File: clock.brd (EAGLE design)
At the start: 100 x 80 mm, 46 parts, among them J3 POWER_JACKSLT, U2 LM75A_SO8, U3 ESP8266_13

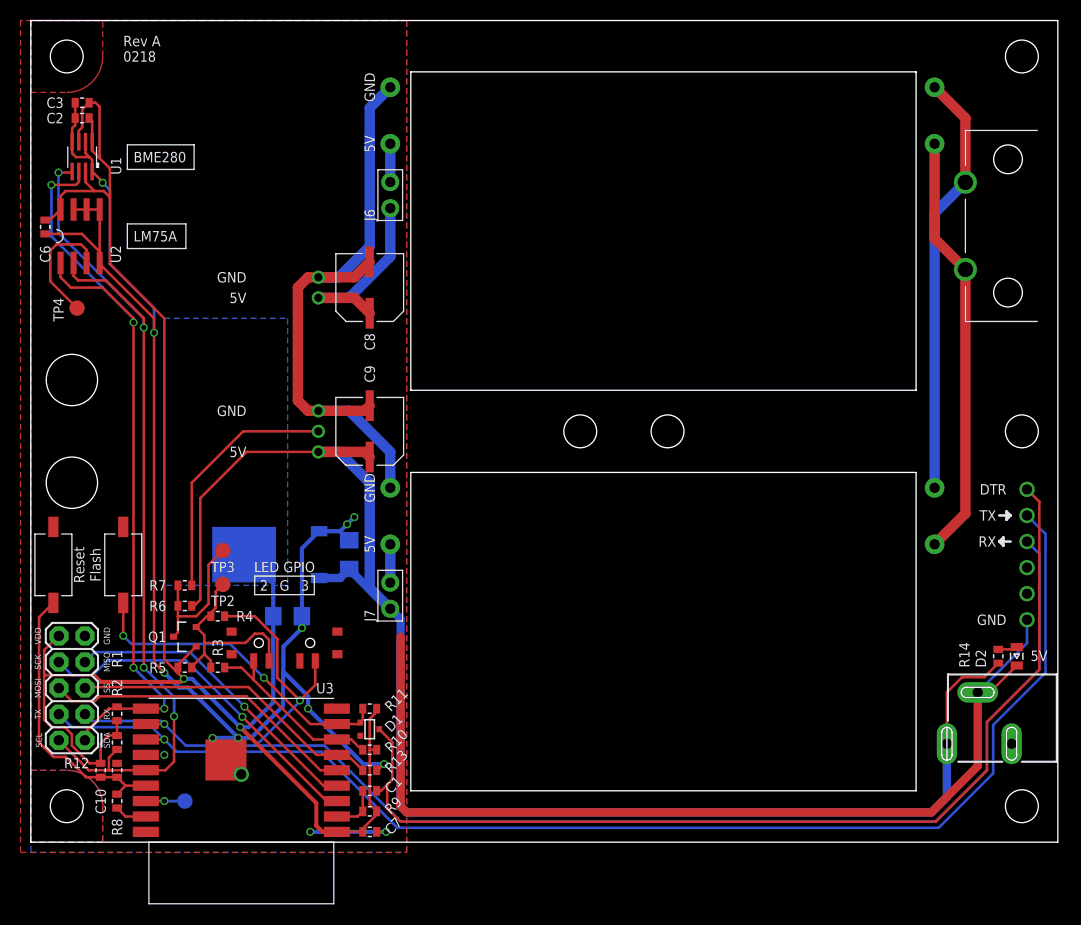
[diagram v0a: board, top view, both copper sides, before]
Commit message: Added a status LED to IO0
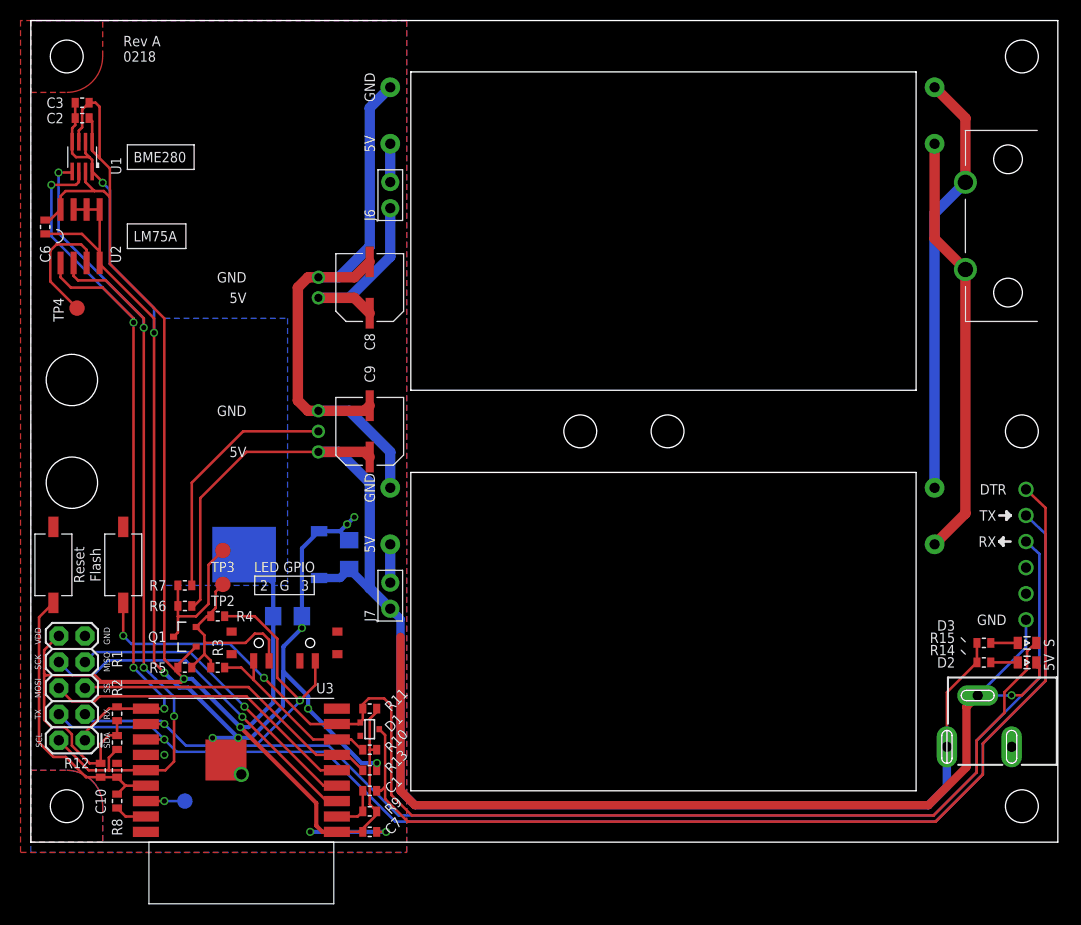
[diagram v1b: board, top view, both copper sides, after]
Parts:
- added D3: (no value), Sebastian:0805_LED
- added R15: 1k, Sebastian:0603
- moved R14 1.52 mm to (92.8, 17.5), turned to 180 degrees
- moved D2 1.17 mm to (97.0, 17.5), turned to 0 degrees
- moved J3 0.30 mm to (103.0, 6.70)
- moved J1 0.10 mm to (96.9, 28.0)
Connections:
- new net N$5: D3.A, R15.1
- net IO0: now also D3.C
- net PVDD: now also R15.2
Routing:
- net IO0: track 31.4 -> 118.4 mm
- net N$5: track 0.00 -> 2.62 mm
- net GND: track 308.5 -> 310.9 mm, vias 16 -> 17
- net PVDD: track 167.4 -> 165.2 mm
- net TXD: track 127.5 -> 126.6 mm
- net RXD: track 144.5 -> 143.6 mm
- net N$4: track 1.89 -> 2.62 mm
- net N$15: track 101.1 -> 100.6 mm
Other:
- board text added: "S"

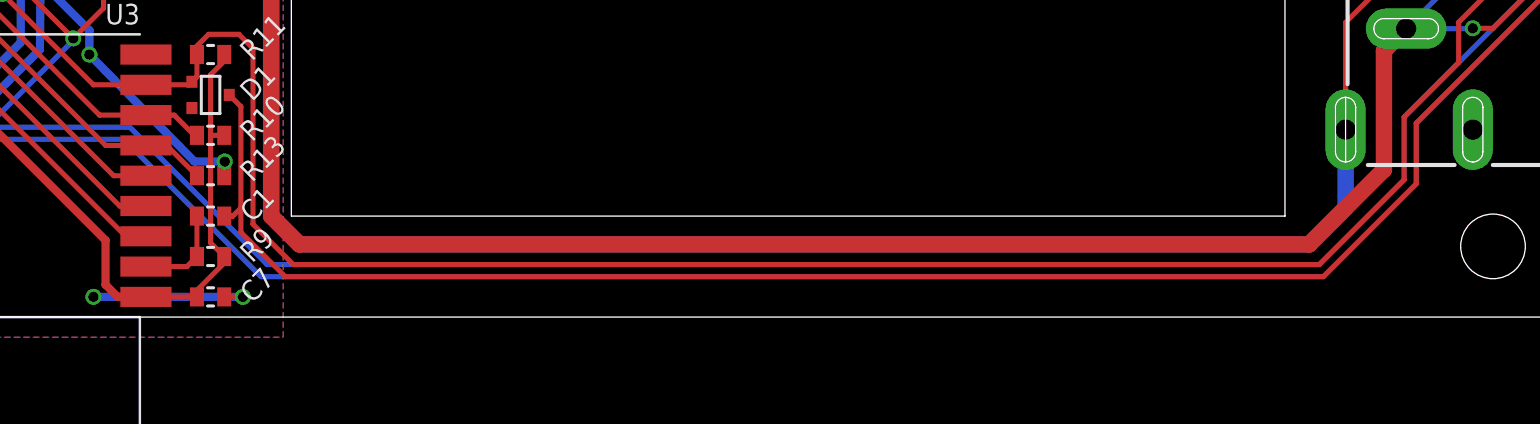
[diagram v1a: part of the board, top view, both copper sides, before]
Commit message: Increased the safety margin between the live side of the power supply and the isolated 5 v rail
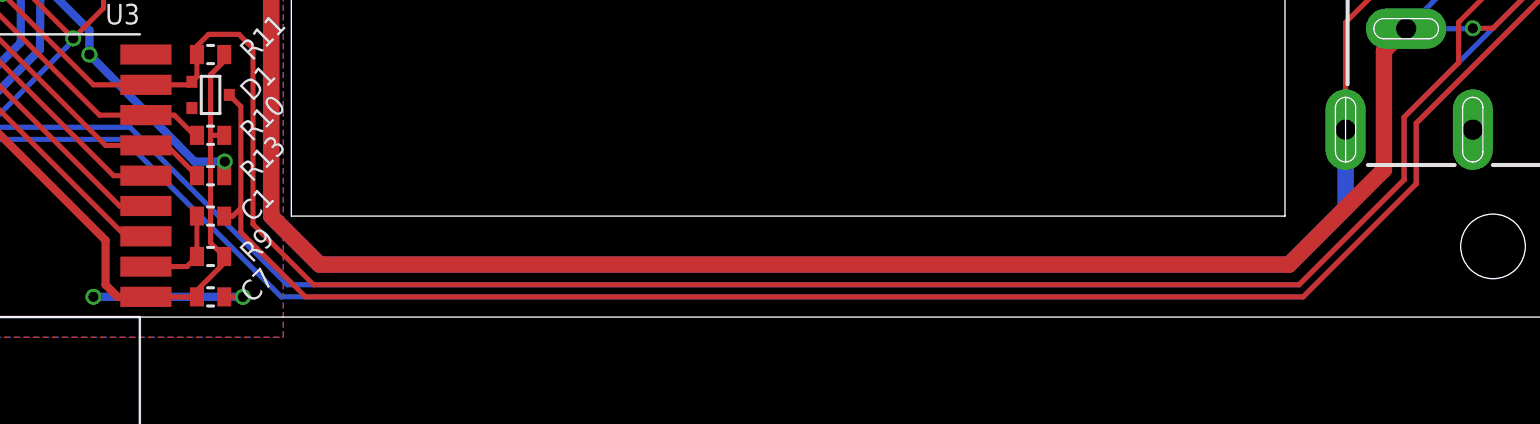
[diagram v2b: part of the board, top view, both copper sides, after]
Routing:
- net PVDD: track 165.2 -> 166.0 mm
- net IO0: track 118.4 -> 119.2 mm
- net GND: track 310.9 -> 311.8 mm
- net TXD: track 126.6 -> 127.4 mm
- net N$15: track 100.6 -> 101.4 mm
- net RXD: track 143.6 -> 144.4 mm
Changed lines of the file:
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@@
 <wire x1="9" y1="20.1" x2="9" y2="23.3" width="0.254" layer="1"/>
 <wire x1="92.1" y1="9.9" x2="92.1" y2="6.8" width="0.254" layer="1"/>
-<wire x1="92.1" y1="6.8" x2="87.9" y2="2.6" width="0.254" layer="1"/>
-<wire x1="87.9" y1="2.6" x2="37.1" y2="2.6" width="0.254" layer="1"/>
+<wire x1="92.1" y1="6.8" x2="86.9" y2="1.6" width="0.254" layer="1"/>
+<wire x1="86.9" y1="1.6" x2="38.1" y2="1.6" width="0.254" layer="1"/>
 <wire x1="35.1" y1="13.3" x2="34.4" y2="14" width="0.254" layer="1"/>
 <wire x1="32.9" y1="14" x2="34.4" y2="14" width="0.254" layer="1"/>
-<wire x1="37.1" y1="2.6" x2="35.1" y2="4.6" width="0.254" layer="1"/>
+<wire x1="38.1" y1="1.6" x2="35.1" y2="4.6" width="0.254" layer="1"/>
 <wire x1="35.1" y1="4.6" x2="35.1" y2="13.3" width="0.254" layer="1"/>
 <wire x1="32.325" y1="13" x2="32.325" y2="13.425" width="0.254" layer="1"/>
@@
 <wire x1="15.1" y1="9.4" x2="21.9" y2="9.4" width="0.254" layer="16"/>
 <wire x1="21.9" y1="9.4" x2="29" y2="9.4" width="0.254" layer="16"/>
-<wire x1="29" y1="9.4" x2="35.8" y2="2.6" width="0.254" layer="16"/>
-<wire x1="35.8" y1="2.6" x2="87.9" y2="2.6" width="0.254" layer="16"/>
-<wire x1="87.9" y1="2.6" x2="92.1" y2="6.8" width="0.254" layer="16"/>
+<wire x1="29" y1="9.4" x2="36.8" y2="1.6" width="0.254" layer="16"/>
+<wire x1="36.8" y1="1.6" x2="86.9" y2="1.6" width="0.254" layer="16"/>
+<wire x1="86.9" y1="1.6" x2="92.1" y2="6.8" width="0.254" layer="16"/>
 <wire x1="92.1" y1="6.8" x2="92.1" y2="9.9" width="0.254" layer="16"/>
 <wire x1="92.1" y1="9.9" x2="98.2" y2="16" width="0.254" layer="16"/>
@@
 <wire x1="13" y1="10" x2="14.2" y2="8.8" width="0.254" layer="16"/>
 <wire x1="14.2" y1="8.8" x2="28.7" y2="8.8" width="0.254" layer="16"/>
-<wire x1="28.7" y1="8.8" x2="35.5" y2="2" width="0.254" layer="16"/>
-<wire x1="35.5" y1="2" x2="88.1" y2="2" width="0.254" layer="16"/>
-<wire x1="88.1" y1="2" x2="92.7" y2="6.6" width="0.254" layer="16"/>
+<wire x1="28.7" y1="8.8" x2="36.5" y2="1" width="0.254" layer="16"/>
+<wire x1="36.5" y1="1" x2="87.1" y2="1" width="0.254" layer="16"/>
+<wire x1="87.1" y1="1" x2="92.7" y2="6.6" width="0.254" layer="16"/>
 <wire x1="92.7" y1="6.6" x2="92.7" y2="9.6" width="0.254" layer="16"/>
 <wire x1="92.7" y1="9.6" x2="98.8" y2="15.7" width="0.254" layer="16"/>
@@
 <wire x1="98.8" y1="15.7" x2="92.7" y2="9.6" width="0.254" layer="1"/>
 <wire x1="92.7" y1="9.6" x2="92.7" y2="6.6" width="0.254" layer="1"/>
-<wire x1="92.7" y1="6.6" x2="88.1" y2="2" width="0.254" layer="1"/>
-<wire x1="88.1" y1="2" x2="36.7" y2="2" width="0.254" layer="1"/>
-<wire x1="36.7" y1="2" x2="34.5" y2="4.2" width="0.254" layer="1"/>
+<wire x1="92.7" y1="6.6" x2="87.1" y2="1" width="0.254" layer="1"/>
+<wire x1="87.1" y1="1" x2="37.7" y2="1" width="0.254" layer="1"/>
+<wire x1="37.7" y1="1" x2="34.5" y2="4.2" width="0.254" layer="1"/>
 <wire x1="34.5" y1="4.2" x2="34.5" y2="5.4" width="0.254" layer="1"/>
 <wire x1="98.8" y1="15.7" x2="98.8" y2="32.55" width="0.254" layer="1"/>
@@
 <wire x1="92.2" y1="14.28" x2="91.1" y2="13.18" width="0.8128" layer="1"/>
 <wire x1="91.1" y1="13.18" x2="91.1" y2="7.3" width="0.8128" layer="1"/>
-<wire x1="91.1" y1="7.3" x2="87.4" y2="3.6" width="0.8128" layer="1"/>
-<wire x1="87.4" y1="3.6" x2="37.4" y2="3.6" width="0.8128" layer="1"/>
-<wire x1="37.4" y1="3.6" x2="36" y2="5" width="0.8128" layer="1"/>
+<wire x1="91.1" y1="7.3" x2="86.4" y2="2.6" width="0.8128" layer="1"/>
+<wire x1="86.4" y1="2.6" x2="38.4" y2="2.6" width="0.8128" layer="1"/>
+<wire x1="38.4" y1="2.6" x2="36" y2="5" width="0.8128" layer="1"/>
 <wire x1="36" y1="5" x2="36" y2="20" width="0.8128" layer="1"/>
 <polygon width="0.254" layer="1" rank="6">
@@
 <contactref element="J3" pad="PWR"/>
 <wire x1="89.2" y1="9.28" x2="89.2" y2="5.4" width="0.8128" layer="16"/>
-<wire x1="89.2" y1="5.4" x2="87.4" y2="3.6" width="0.8128" layer="16"/>
-<wire x1="87.4" y1="3.6" x2="37.4" y2="3.6" width="0.8128" layer="16"/>
-<wire x1="37.4" y1="3.6" x2="36" y2="5" width="0.8128" layer="16"/>
+<wire x1="89.2" y1="5.4" x2="86.4" y2="2.6" width="0.8128" layer="16"/>
+<wire x1="86.4" y1="2.6" x2="38.4" y2="2.6" width="0.8128" layer="16"/>
+<wire x1="38.4" y1="2.6" x2="36" y2="5" width="0.8128" layer="16"/>
 <wire x1="33" y1="37.5" x2="32.5" y2="38" width="1.016" layer="1"/>
 <wire x1="32.5" y1="38" x2="28" y2="38" width="1.016" layer="1"/>

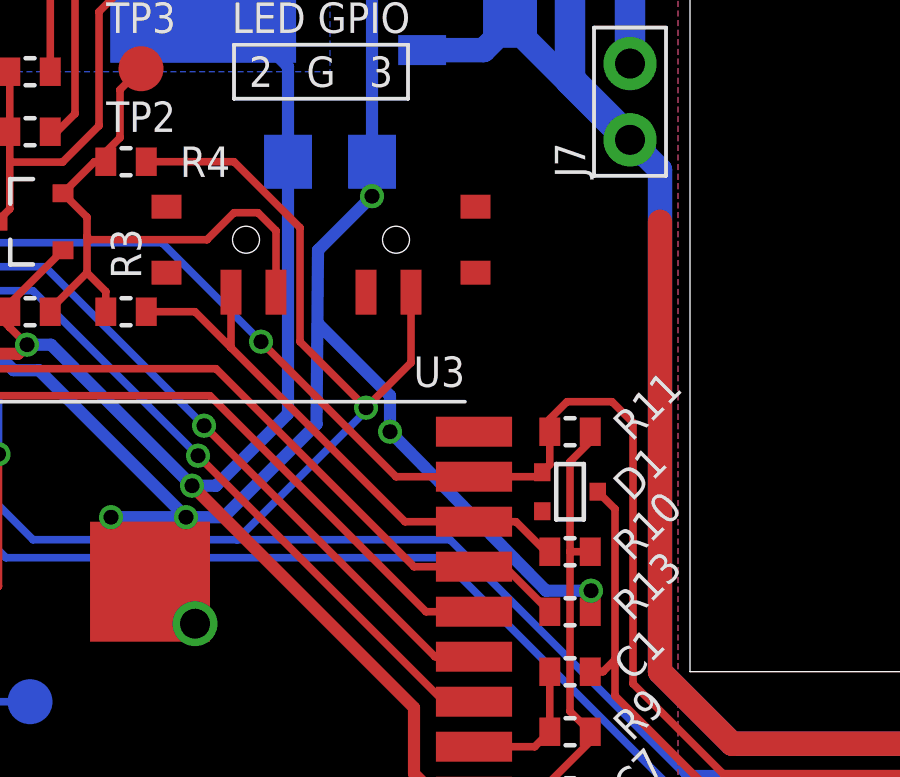
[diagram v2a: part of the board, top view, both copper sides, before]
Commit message: Added testpoints to IO2 and IO3
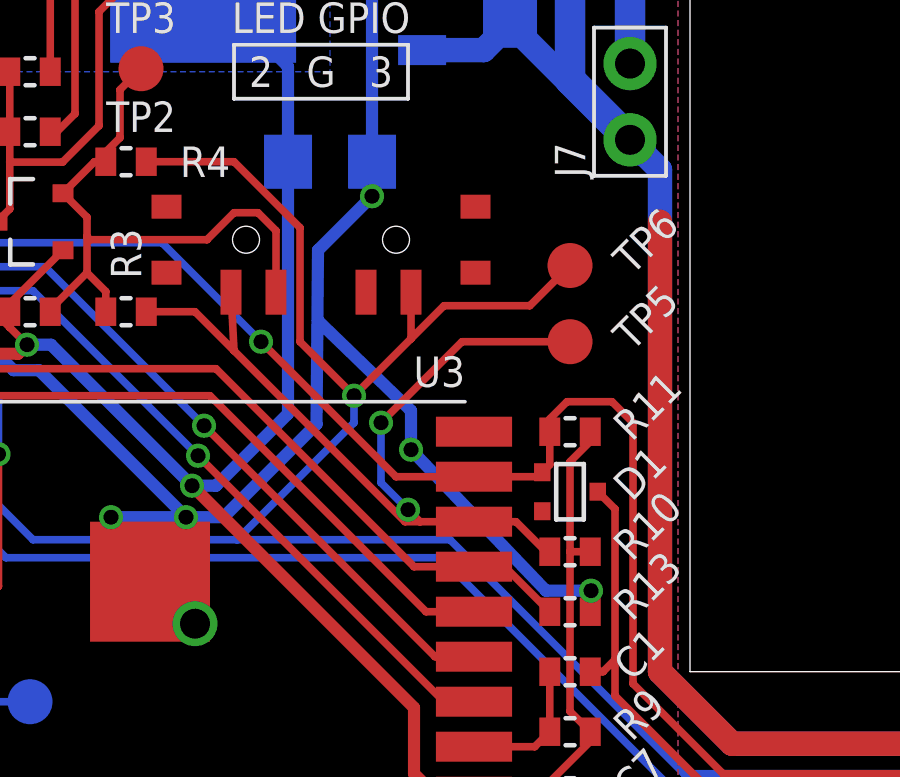
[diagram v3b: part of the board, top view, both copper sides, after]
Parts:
- added TP5, TP6: TPTP15R, testpad:TP15R
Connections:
- net IO2: now also TP5.TP
- net RXD: now also TP6.TP
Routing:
- net IO2: track 18.6 -> 30.0 mm, vias 0 -> 2
- net RXD: track 144.4 -> 150.2 mm
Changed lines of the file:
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@@
 <attribute name="NAME" x="90" y="19.9" size="1.016" layer="25" font="vector" ratio="12" rot="R180" align="center-left"/>
+</element>
+<element name="TP5" library="testpad" package="TP15R" value="TPTP15R" x="33" y="16" smashed="yes">
+<attribute name="NAME" x="34.7" y="16" size="1.016" layer="25" font="vector" ratio="12" rot="R45" align="center-left"/>
+<attribute name="TP_SIGNAL_NAME" value="" x="33" y="13.46" size="1" layer="37"/>
+<attribute name="VALUE" x="32.365" y="15.238" size="0.0254" layer="27"/>
+</element>
+<element name="TP6" library="testpad" package="TP15R" value="TPTP15R" x="33" y="18.54" smashed="yes">
+<attribute name="NAME" x="34.7" y="18.54" size="1.016" layer="25" font="vector" ratio="12" rot="R45" align="center-left"/>
+<attribute name="TP_SIGNAL_NAME" value="" x="33" y="16" size="1" layer="37"/>
+<attribute name="VALUE" x="32.365" y="17.778" size="0.0254" layer="27"/>
 </element>
 </elements>
@@
 <wire x1="32.2" y1="9" x2="32.325" y2="9" width="0.254" layer="1"/>
 <wire x1="29.8" y1="10" x2="31.2" y2="10" width="0.254" layer="1"/>
-<wire x1="29.8" y1="10" x2="27.5" y2="10" width="0.254" layer="1"/>
-<wire x1="27.5" y1="10" x2="21.7" y2="15.8" width="0.254" layer="1"/>
+<wire x1="29.8" y1="10" x2="28" y2="10" width="0.254" layer="1"/>
+<wire x1="28" y1="10" x2="27.5" y2="10" width="0.254" layer="1"/>
 <contactref element="R3" pad="1"/>
 <contactref element="U$1" pad="4"/>
-<wire x1="21.7" y1="17.65" x2="21.7" y2="15.8" width="0.254" layer="1"/>
+<wire x1="27.5" y1="10" x2="21.8" y2="15.7" width="0.254" layer="1"/>
+<wire x1="21.7" y1="17.65" x2="21.8" y2="15.7" width="0.254" layer="1"/>
 <wire x1="18.875" y1="17" x2="20.5" y2="17" width="0.254" layer="1"/>
-<wire x1="20.5" y1="17" x2="21.7" y2="15.8" width="0.254" layer="1"/>
+<wire x1="20.5" y1="17" x2="21.8" y2="15.7" width="0.254" layer="1"/>
+<contactref element="TP5" pad="TP"/>
+<via x="27.6" y="10.4" extent="1-16" drill="0.5"/>
+<wire x1="27.6" y1="10.4" x2="26.7" y2="11.3" width="0.254" layer="16"/>
+<wire x1="26.7" y1="11.3" x2="26.7" y2="13.3" width="0.254" layer="16"/>
+<via x="26.7" y="13.3" extent="1-16" drill="0.5"/>
+<wire x1="27.6" y1="10.4" x2="28" y2="10" width="0.254" layer="1"/>
+<wire x1="26.7" y1="13.3" x2="29.4" y2="16" width="0.254" layer="1"/>
+<wire x1="29.4" y1="16" x2="33" y2="16" width="0.254" layer="1"/>
 </signal>
 <signal name="EN">
@@
 <wire x1="12.7" y1="11.8" x2="5.93" y2="11.8" width="0.254" layer="16"/>
 <contactref element="R4" pad="1"/>
-<via x="26.2" y="13.8" extent="1-16" drill="0.5"/>
-<wire x1="26.2" y1="13.8" x2="26.2" y2="13.7" width="0.254" layer="16"/>
-<wire x1="26.2" y1="13.7" x2="21.9" y2="9.4" width="0.254" layer="16"/>
+<via x="25.8" y="14.2" extent="1-16" drill="0.5"/>
+<wire x1="25.8" y1="14.2" x2="25.8" y2="13.3" width="0.254" layer="16"/>
+<wire x1="25.8" y1="13.3" x2="21.9" y2="9.4" width="0.254" layer="16"/>
 <contactref element="U$1" pad="1"/>
-<wire x1="27.7" y1="17.65" x2="27.7" y2="15.3" width="0.254" layer="1"/>
-<wire x1="27.7" y1="15.3" x2="26.2" y2="13.8" width="0.254" layer="1"/>
+<wire x1="27.7" y1="17.65" x2="27.7" y2="16.1" width="0.254" layer="1"/>
+<wire x1="27.7" y1="16.1" x2="25.8" y2="14.2" width="0.254" layer="1"/>
 <wire x1="18.875" y1="22" x2="21.8" y2="22" width="0.254" layer="1"/>
 <wire x1="21.8" y1="22" x2="24" y2="19.8" width="0.254" layer="1"/>
 <wire x1="24" y1="19.8" x2="24" y2="16" width="0.254" layer="1"/>
-<wire x1="24" y1="16" x2="26.2" y2="13.8" width="0.254" layer="1"/>
+<wire x1="24" y1="16" x2="25.8" y2="14.2" width="0.254" layer="1"/>
+<contactref element="TP6" pad="TP"/>
+<wire x1="33" y1="18.54" x2="31.66" y2="17.2" width="0.254" layer="1"/>
+<wire x1="28.8" y1="17.2" x2="27.7" y2="16.1" width="0.254" layer="1"/>
+<wire x1="31.66" y1="17.2" x2="28.8" y2="17.2" width="0.254" layer="1"/>
 </signal>
 <signal name="TXD">
@@
 <wire x1="34.6" y1="1" x2="27.2" y2="1" width="0.4064" layer="16"/>
 <wire x1="33.7" y1="7.7" x2="32.2" y2="7.7" width="0.4064" layer="16"/>
-<wire x1="32.2" y1="7.7" x2="27" y2="13" width="0.4064" layer="16"/>
-<via x="27" y="13" extent="1-16" drill="0.5"/>
+<wire x1="32.2" y1="7.7" x2="27.7" y2="12.4" width="0.4064" layer="16"/>
+<via x="27.7" y="12.4" extent="1-16" drill="0.5"/>
 <contactref element="U2" pad="7"/>
 <contactref element="U2" pad="6"/>
@@
 <contactref element="U$1" pad="CASE1" route="any" routetag="G$1.GND"/>
 <contactref element="U$1" pad="2"/>
-<wire x1="27" y1="13" x2="27" y2="14.2" width="0.4064" layer="16"/>
-<wire x1="27" y1="14.2" x2="24.6" y2="16.6" width="0.4064" layer="16"/>
+<wire x1="27.7" y1="12.4" x2="27.7" y2="13.7" width="0.4064" layer="16"/>
+<wire x1="27.7" y1="13.7" x2="24.6" y2="16.7" width="0.4064" layer="16"/>
 <polygon width="0.254" layer="16" rank="6">
 <vertex x="36.6" y="-1"/>
